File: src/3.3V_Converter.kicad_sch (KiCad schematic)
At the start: 16 parts, among them U4 TPS566238RQFR (12V-3.3V)

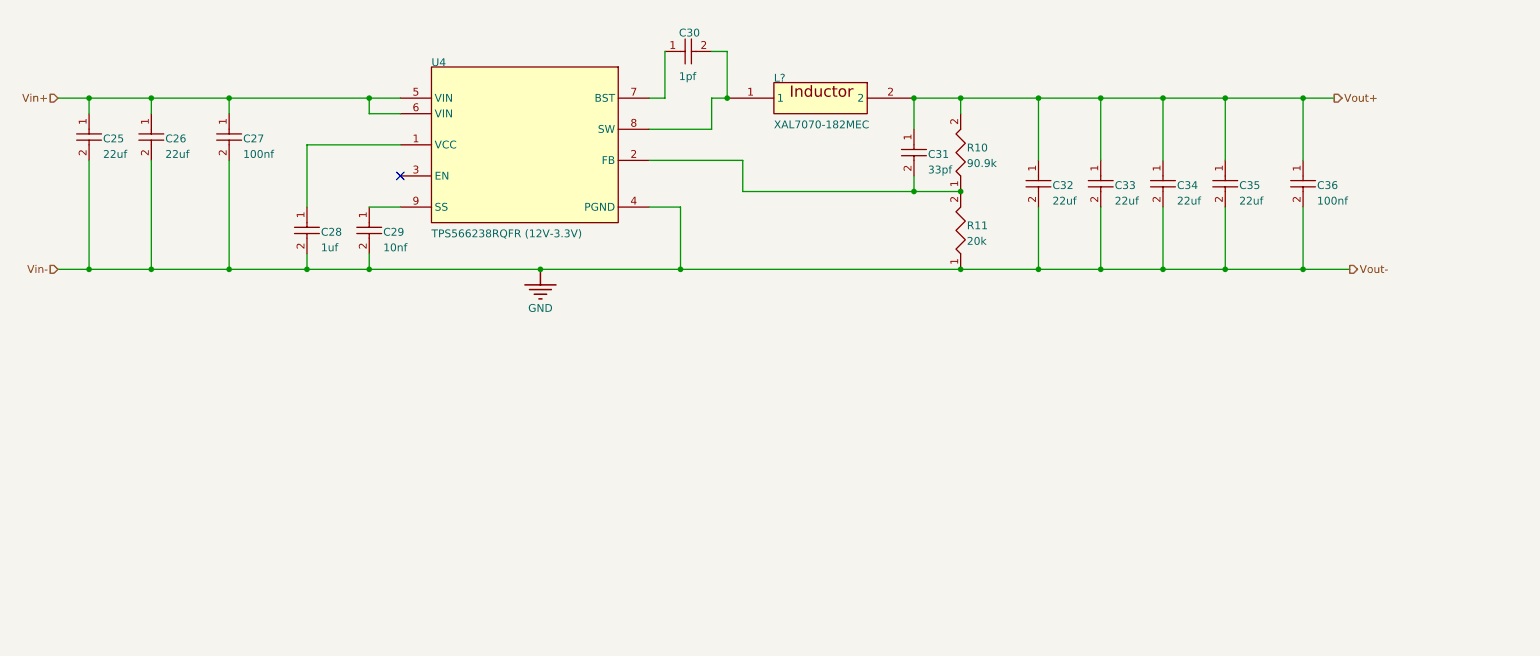
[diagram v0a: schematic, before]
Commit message: Updated majority of passive components to KiCad format
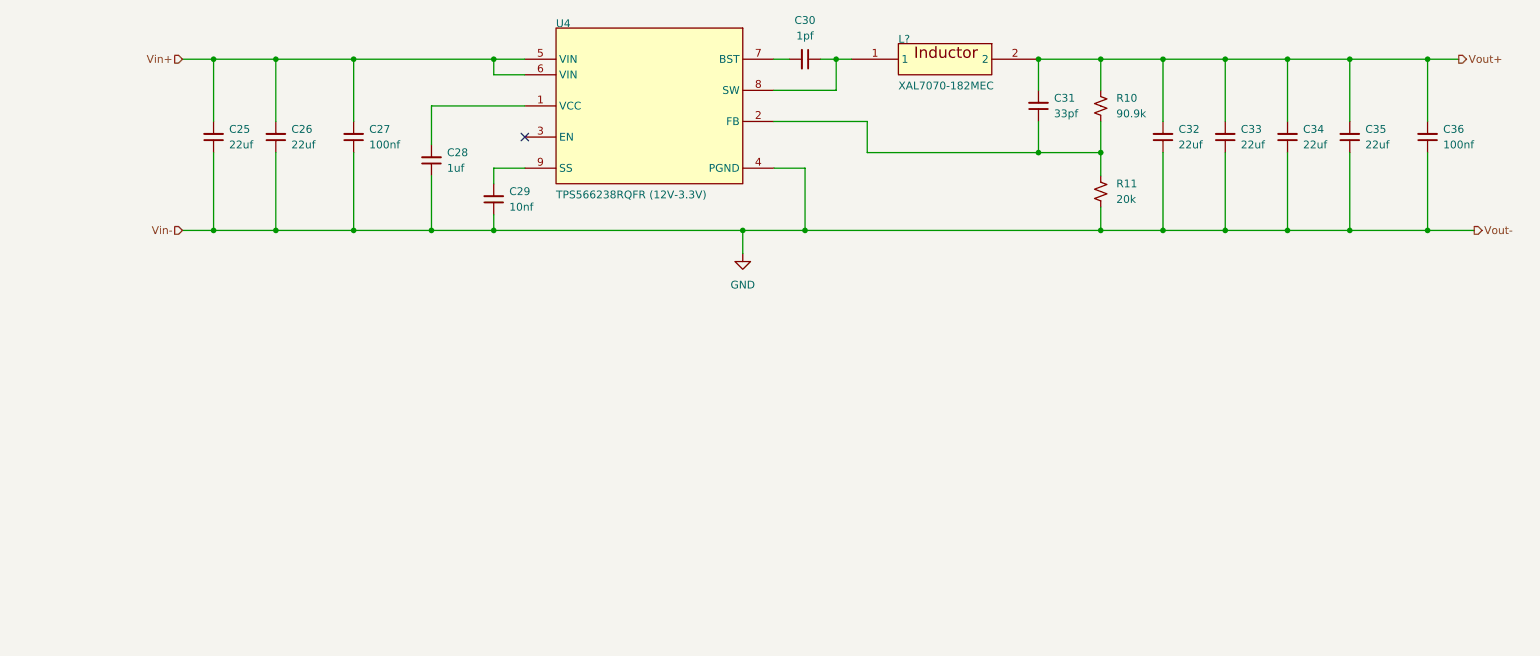
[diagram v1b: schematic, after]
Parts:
- removed C25, C26, C32, C33, C34, C35: Capacitor 1 uF +/- 10% 50 V 0805, powerDristributionBoard-import-fps:CAPC2013X135X45NL10T25, symbol Autonomous Vehicle Lab:CAP-NP-2
- removed C27, C28, C31, C36: Capacitor 10µF +/-20% 10V 0603, powerDristributionBoard-import-fps:CAPC0603(1608)100_L, symbol Autonomous Vehicle Lab:CAP-NP-2
- removed C29, C30: Capacitor 10 pF +/- 0.25 pF 50 V 0402, powerDristributionBoard-import-fps:CAPC1005X55X30LL05T10, symbol Autonomous Vehicle Lab:CAP-NP-2
- removed R10, R11: Resistor 1K +/-5% 0805 125 mW, powerDristributionBoard-import-fps:RESC0805(2012)_L, symbol Autonomous Vehicle Lab:RES-2
- added C25, C26, C32, C33, C34, C35: 22uf, Capacitor_SMD:C_0805_2012Metric, symbol Device:C_Small
- added C27, C36: 100nf, Capacitor_SMD:C_0603_1608Metric, symbol Device:C_Small
- added C28: 1uf, Capacitor_SMD:C_0603_1608Metric, symbol Device:C_Small
- added C29: 10nf, Capacitor_SMD:C_0402_1005Metric, symbol Device:C_Small
- added C30: 1pf, Capacitor_SMD:C_0402_1005Metric, symbol Device:C_Small
- added C31: 33pf, Capacitor_SMD:C_0603_1608Metric, symbol Device:C_Small
- added R10: 90.9k, Resistor_SMD:R_0805_2012Metric, symbol Device:R_Small_US
- added R11: 20k, Resistor_SMD:R_0805_2012Metric, symbol Device:R_Small_US
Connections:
- net GND: now also C25.1, C26.1, C27.1, C28.1, C29.1, C32.1, C33.1, C34.1, C35.1, C36.1, R11.2
- net Vin+: now also C25.2, C26.2, C27.2
- net Vout+: now also C31.2, C32.2, C33.2, C34.2, C35.2, C36.2, R10.1
- net at U4.2 (FB): now also C31.1, R10.2, R11.1
- net at U4.1 (VCC): now also C28.2
- net at U4.7 (BST): now also C30.2
- net at L?.1, U4.8 (SW): now also C30.1
- net at U4.9 (SS): now also C29.2
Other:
- moved on the sheet: L?, U4

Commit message: edit 3.3
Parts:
- added R1, R2: R_Small_US, symbol Device:R_Small_US
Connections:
- net GND: now also R1.1
- new net: R1.2, R2.1
